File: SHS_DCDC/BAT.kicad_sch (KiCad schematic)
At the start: 11 parts, among them Q10 PMV100XPEAR, Q11 PMV100XPEAR, Q12 PMV100XPEAR, Q17 MOSP_GENERIC, Q9 PMV100XPEAR, U2 INA181, U7 MCP101

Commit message: Ubuntu transfer
Commit before transfer onto Ubuntu
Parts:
- removed Q17: MOSP_GENERIC, Package_TO_SOT_SMD:SOT-23, symbol SHS_DCDC:MOSP_GENERIC
- added Q17: PMV100XPEAR, digikey-kicad-library-master:SOT-23-3, symbol SHS_DCDC:PMV100XPEAR
- Q12: footprint digikey-footprints:SOT-23-3 -> digikey-kicad-library-master:SOT-23-3
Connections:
- net ODP_RESET: now also Q17.1 (G)
- net VBAT: now also Q17.2 (S)
- net at R8.1, U2.3 (+): now also Q17.3 (D)
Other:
- note added: "THAT VOLTAGE DETECTOR SENSE THE BATTERY'S VOLTAGE. IF VBAT GOES BELOW A CERTAIN VOLTAGE, IT TRIGGERS A POSITIVE VALUE. THAT POSITIVE VALUE BLOCKS THE DRAIN OF THE BATTERY."
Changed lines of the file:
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@@
     (stroke (width 0) (type default) (color 0 0 0 0))
   )
-  (wire (pts (xy 198.12 118.11) (xy 209.55 118.11))
+  (wire (pts (xy 198.12 120.65) (xy 208.28 120.65))
     (stroke (width 0) (type default) (color 0 0 0 0))
   )
@@
     (stroke (width 0) (type default) (color 0 0 0 0))
   )
-  (wire (pts (xy 217.17 97.79) (xy 217.17 115.57))
+  (wire (pts (xy 217.17 97.79) (xy 217.17 113.03))
     (stroke (width 0) (type default) (color 0 0 0 0))
   )
@@
     (stroke (width 0) (type default) (color 0 0 0 0))
   )
-  (wire (pts (xy 217.17 125.73) (xy 217.17 137.16))
+  (wire (pts (xy 217.17 123.19) (xy 217.17 137.16))
     (stroke (width 0) (type default) (color 0 0 0 0))
   )
@@
     (effects (font (size 1.27 1.27)) (justify left bottom))
   )
+  (text "THAT VOLTAGE DETECTOR SENSE THE BATTERY'S VOLTAGE.\nIF VBAT GOES BELOW A CERTAIN VOLTAGE, IT TRIGGERS A POSITIVE VALUE.\nTHAT POSITIVE VALUE BLOCKS THE DRAIN OF THE BATTERY."
+    (at 80.01 43.18 0)
+    (effects (font (size 1.27 1.27)) (justify left bottom))
+  )
   (text "INSTRUM AMPLIFIER BLOCK\nVREF_BIDIRECTIONAL IS HALF THE VDD OF THE MCU\nTHAT MEANS THE OUTPUT VALUE WILL VARY AROUND THAT EQUILIBRIUM POINT\nBELOW OR HIGHER THAN VDD/2 WILL DEFINE BIDIRECTIONALITY OF THE BATTERY CURRENT\nEG, IF THE BATTERY IS DISCHARGING OR CHARGING\nSEE INA181 DATASHEET FOR MORE INFO"
     (at 146.05 58.42 0)
     (effects (font (size 1.27 1.27)) (justify left bottom))
   )
-  (global_label "USB_IN" (shape input) (at 262.89 46.99 0) (fields_autoplaced)
+  (global_label "USB_IN" (shape input) (at 261.62 46.99 0) (fields_autoplaced)
     (effects (font (size 1.27 1.27)) (justify left))
-    (property "Intersheet References" "${INTERSHEET_REFS}" (id 0) (at 288.29 -176.53 0)
+    (property "Intersheet References" "${INTERSHEET_REFS}" (id 0) (at 287.02 -176.53 0)
       (effects (font (size 1.27 1.27)) hide)
     )
@@
     )
   )
-  (global_label "ODP_RESET" (shape input) (at 198.12 118.11 180) (fields_autoplaced)
+  (global_label "ODP_RESET" (shape input) (at 198.12 120.65 180) (fields_autoplaced)
     (effects (font (size 1.27 1.27)) (justify right))
-    (property "Intersheet References" "${INTERSHEET_REFS}" (id 0) (at 185.2125 118.0306 0)
+    (property "Intersheet References" "${INTERSHEET_REFS}" (id 0) (at 185.2125 120.5706 0)
       (effects (font (size 1.27 1.27)) (justify right) hide)
     )
@@
       (effects (font (size 1.524 1.524)) (justify left))
     )
-    (property "Footprint" "digikey-footprints:SOT-23-3" (id 2) (at 110.49 129.54 0)
+    (property "Footprint" "digikey-kicad-library-master:SOT-23-3" (id 2) (at 110.49 129.54 0)
       (effects (font (size 1.524 1.524)) (justify left) hide)
     )
@@
     )
     (pin "1")
+  )
+  (symbol (lib_id "SHS_DCDC:PMV100XPEAR") (at 217.17 118.11 0) (unit 1)
+    (in_bom yes) (on_board yes) (fields_autoplaced)
+    (property "Reference" "Q17" (id 0) (at 220.98 118.2997 0)
+      (effects (font (size 1.524 1.524)) (justify left))
+    )
+    (property "Value" "PMV100XPEAR" (id 1) (at 220.98 122.1097 0)
+      (effects (font (size 1.524 1.524)) (justify left))
+    )
+    (property "Footprint" "digikey-kicad-library-master:SOT-23-3" (id 2) (at 222.25 113.03 0)
+      (effects (font (size 1.524 1.524)) (justify left) hide)
+    )
+    (property "Datasheet" "" (id 3) (at 222.25 110.49 0)
+      (effects (font (size 1.524 1.524)) (justify left) hide)
+    )
+    (property "MPN" "PMV100XPEAR" (id 4) (at 222.25 105.41 0)
+      (effects (font (size 1.524 1.524)) (justify left) hide)
+    )
+    (property "Category" "Discrete Semiconductor Products" (id 5) (at 222.25 102.87 0)
+      (effects (font (size 1.524 1.524)) (justify left) hide)
+    )
+    (property "Family" "Transistors - FETs, MOSFETs - Single" (id 6) (at 222.25 100.33 0)
+      (effects (font (size 1.524 1.524)) (justify left) hide)
+    )
+    (property "Description" "MOSFET P-CH 20V 2.4A SOT23" (id 7) (at 222.25 97.79 0)
+      (effects (font (size 1.524 1.524)) (justify left) hide)
+    )
+    (property "Manufacturer" "Nexperia USA" (id 8) (at 222.25 95.25 0)
+      (effects (font (size 1.524 1.524)) (justify left) hide)
+    )
+    (property "Status" "Active" (id 9) (at 222.25 92.71 0)
+      (effects (font (size 1.524 1.524)) (justify left) hide)
+    )
+    (pin "1")
+    (pin "2")
+    (pin "3")
   )
   (symbol (lib_id "SHS_DCDC:C-Device") (at 55.88 44.45 0) (unit 1)
@@
     (pin "1")
   )
-  (symbol (lib_id "SHS_DCDC:MOSP_GENERIC") (at 217.17 120.65 0) (mirror x) (unit 1)
-    (in_bom yes) (on_board yes) (fields_autoplaced)
-    (property "Reference" "Q17" (id 0) (at 220.98 119.38 0)
-      (effects (font (size 1.524 1.524)) (justify left))
-    )
-    (property "Value" "MOSP_GENERIC" (id 1) (at 220.98 123.19 0)
-      (effects (font (size 1.524 1.524)) (justify left))
-    )
-    (property "Footprint" "Package_TO_SOT_SMD:SOT-23" (id 2) (at 222.25 125.73 0)
-      (effects (font (size 1.524 1.524)) (justify left) hide)
-    )
-    (property "Datasheet" "https://www.onsemi.com/pub/Collateral/NDS7002A-D.PDF" (id 3) (at 222.25 128.27 0)
-      (effects (font (size 1.524 1.524)) (justify left) hide)
-    )
-    (property "Digi-Key_PN" "2N7002NCT-ND" (id 4) (at 222.25 130.81 0)
-      (effects (font (size 1.524 1.524)) (justify left) hide)
-    )
-    (property "MPN" "2N7002" (id 5) (at 222.25 133.35 0)
-      (effects (font (size 1.524 1.524)) (justify left) hide)
-    )
-    (property "Category" "Discrete Semiconductor Products" (id 6) (at 222.25 135.89 0)
-      (effects (font (size 1.524 1.524)) (justify left) hide)
-    )
-    (property "Family" "Transistors - FETs, MOSFETs - Single" (id 7) (at 222.25 138.43 0)
-      (effects (font (size 1.524 1.524)) (justify left) hide)
-    )
-    (property "DK_Datasheet_Link" "https://www.onsemi.com/pub/Collateral/NDS7002A-D.PDF" (id 8) (at 222.25 140.97 0)
-      (effects (font (size 1.524 1.524)) (justify left) hide)
-    )
-    (property "DK_Detail_Page" "/product-detail/en/on-semiconductor/2N7002/2N7002NCT-ND/244664" (id 9) (at 222.25 143.51 0)
-      (effects (font (size 1.524 1.524)) (justify left) hide)
-    )
-    (property "Description" "MOSFET N-CH 60V 115MA SOT-23" (id 10) (at 222.25 146.05 0)
-      (effects (font (size 1.524 1.524)) (justify left) hide)
-    )
-    (property "Manufacturer" "ON Semiconductor" (id 11) (at 222.25 148.59 0)
-      (effects (font (size 1.524 1.524)) (justify left) hide)
-    )
-    (property "Status" "Active" (id 12) (at 222.25 151.13 0)
-      (effects (font (size 1.524 1.524)) (justify left) hide)
-    )
-    (pin "1")
-    (pin "2")
-    (pin "3")
-  )
   (symbol (lib_id "SHS_DCDC:GND-power") (at 55.88 54.61 0) (unit 1)

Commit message: Commit_190223
Normal commit
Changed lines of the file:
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@@
   (junction (at 217.17 76.2) (diameter 0) (color 0 0 0 0)
   )
-  (junction (at 233.68 30.48) (diameter 0) (color 0 0 0 0)
-  )
-  (junction (at 217.17 30.48) (diameter 0) (color 0 0 0 0)
-  )
   (junction (at 55.88 36.83) (diameter 0) (color 0 0 0 0)
   )
@@
     (stroke (width 0) (type default) (color 0 0 0 0))
   )
-  (wire (pts (xy 261.62 46.99) (xy 233.68 46.99))
-    (stroke (width 0) (type default) (color 0 0 0 0))
-  )
   (wire (pts (xy 217.17 76.2) (xy 217.17 83.82))
     (stroke (width 0) (type default) (color 0 0 0 0))
@@
     (stroke (width 0) (type default) (color 0 0 0 0))
   )
-  (wire (pts (xy 35.56 30.48) (xy 217.17 30.48))
-    (stroke (width 0) (type default) (color 0 0 0 0))
-  )
   (wire (pts (xy 55.88 48.26) (xy 55.88 54.61))
     (stroke (width 0) (type default) (color 0 0 0 0))
@@
     (stroke (width 0) (type default) (color 0 0 0 0))
   )
-  (wire (pts (xy 217.17 30.48) (xy 233.68 30.48))
-    (stroke (width 0) (type default) (color 0 0 0 0))
-  )
   (wire (pts (xy 95.25 171.45) (xy 95.25 181.61))
     (stroke (width 0) (type default) (color 0 0 0 0))
@@
     (stroke (width 0) (type default) (color 0 0 0 0))
   )
-  (wire (pts (xy 233.68 30.48) (xy 262.89 30.48))
-    (stroke (width 0) (type default) (color 0 0 0 0))
-  )
   (wire (pts (xy 115.57 151.13) (xy 95.25 151.13))
     (stroke (width 0) (type default) (color 0 0 0 0))
@@
   )
   (wire (pts (xy 46.99 151.13) (xy 64.77 151.13))
-    (stroke (width 0) (type default) (color 0 0 0 0))
-  )
-  (wire (pts (xy 233.68 46.99) (xy 233.68 30.48))
     (stroke (width 0) (type default) (color 0 0 0 0))
   )
@@
     (at 146.05 58.42 0)
     (effects (font (size 1.27 1.27)) (justify left bottom))
-  )
-  (global_label "USB_IN" (shape input) (at 261.62 46.99 0) (fields_autoplaced)
-    (effects (font (size 1.27 1.27)) (justify left))
-    (property "Intersheet References" "${INTERSHEET_REFS}" (id 0) (at 287.02 -176.53 0)
-      (effects (font (size 1.27 1.27)) hide)
-    )
   )
   (global_label "VREF_BIDIRECTIONAL" (shape input) (at 133.35 72.39 180) (fields_autoplaced)
@@
     )
   )
-  (global_label "LOAD" (shape output) (at 262.89 30.48 0) (fields_autoplaced)
-    (effects (font (size 1.27 1.27)) (justify left))
-    (property "Intersheet References" "${INTERSHEET_REFS}" (id 0) (at 0 -7.62 0)
-      (effects (font (size 1.27 1.27)) hide)
-    )
-  )
   (global_label "V_MCU" (shape input) (at 152.4 104.14 270) (fields_autoplaced)
     (effects (font (size 1.27 1.27)) (justify right))
@@
     )
   )
-  (global_label "V1" (shape input) (at 35.56 30.48 180) (fields_autoplaced)
-    (effects (font (size 1.27 1.27)) (justify right))
-    (property "Intersheet References" "${INTERSHEET_REFS}" (id 0) (at 30.9377 30.4006 0)
-      (effects (font (size 1.27 1.27)) (justify right) hide)
-    )
-  )
+  (global_label "LOAD" (shape input) (at 217.17 30.48 90) (fields_autoplaced)
+    (effects (font (size 1.27 1.27)) (justify left))
+    (property "Intersheet References" "${INTERSHEET_REFS}" (id 0) (at 217.2494 23.4387 90)
+      (effects (font (size 1.27 1.27)) (justify left) hide)
+    )
+  )

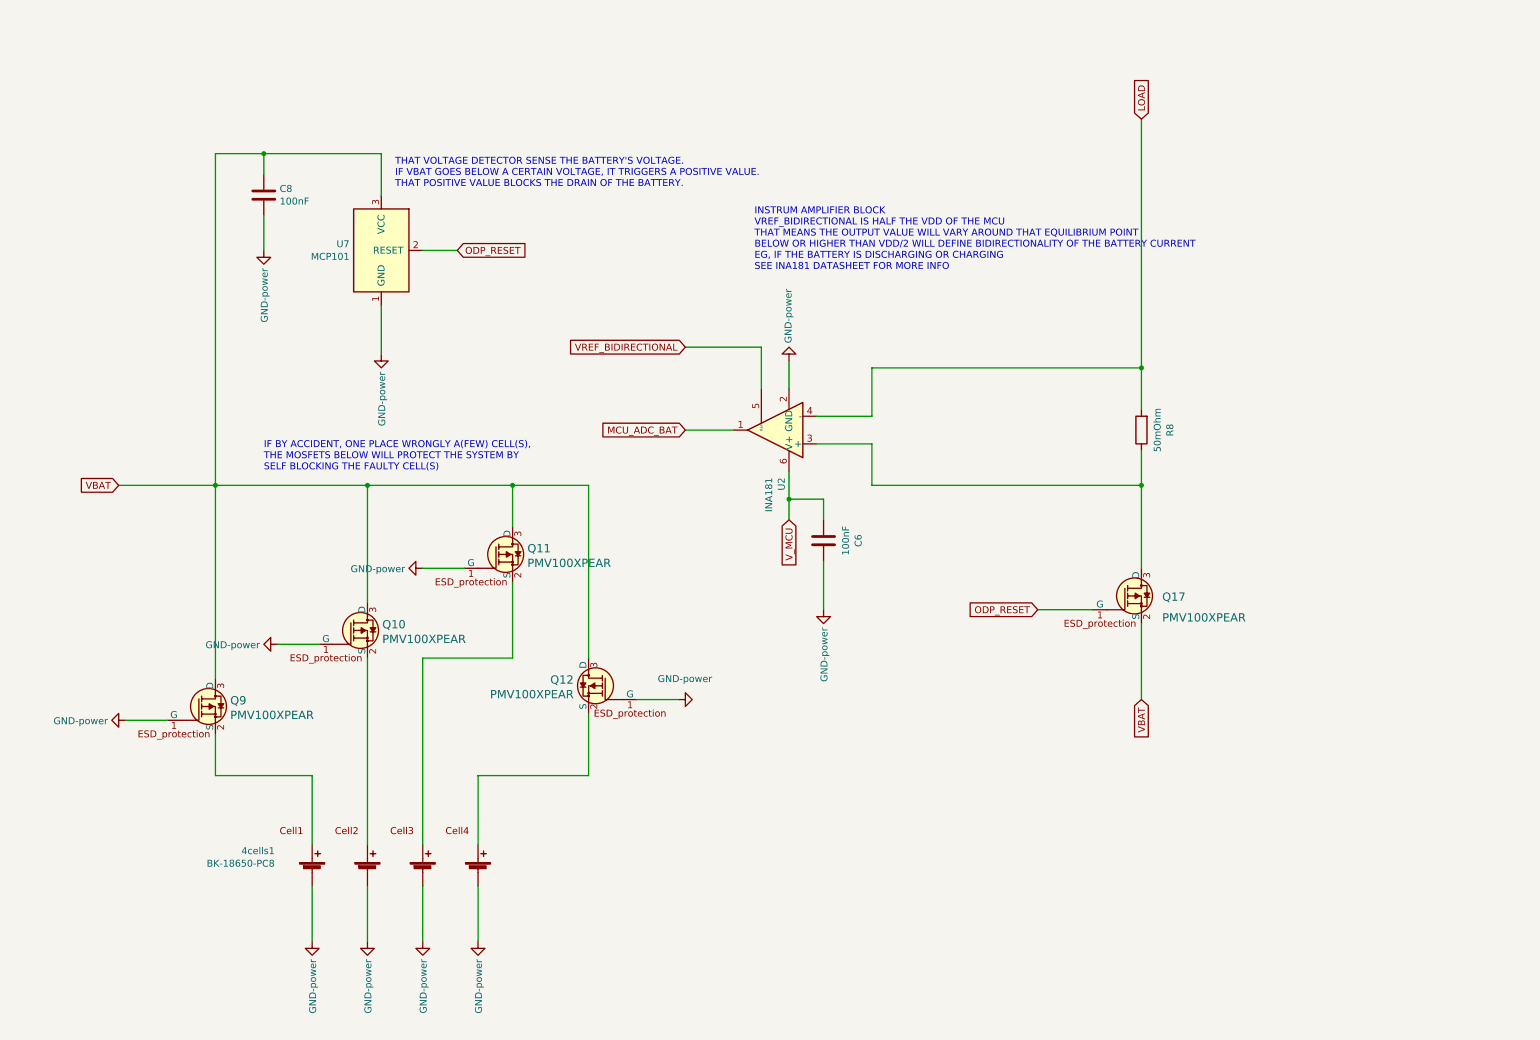
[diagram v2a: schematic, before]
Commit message: Commit_Fix
Fix to move back to ESP32
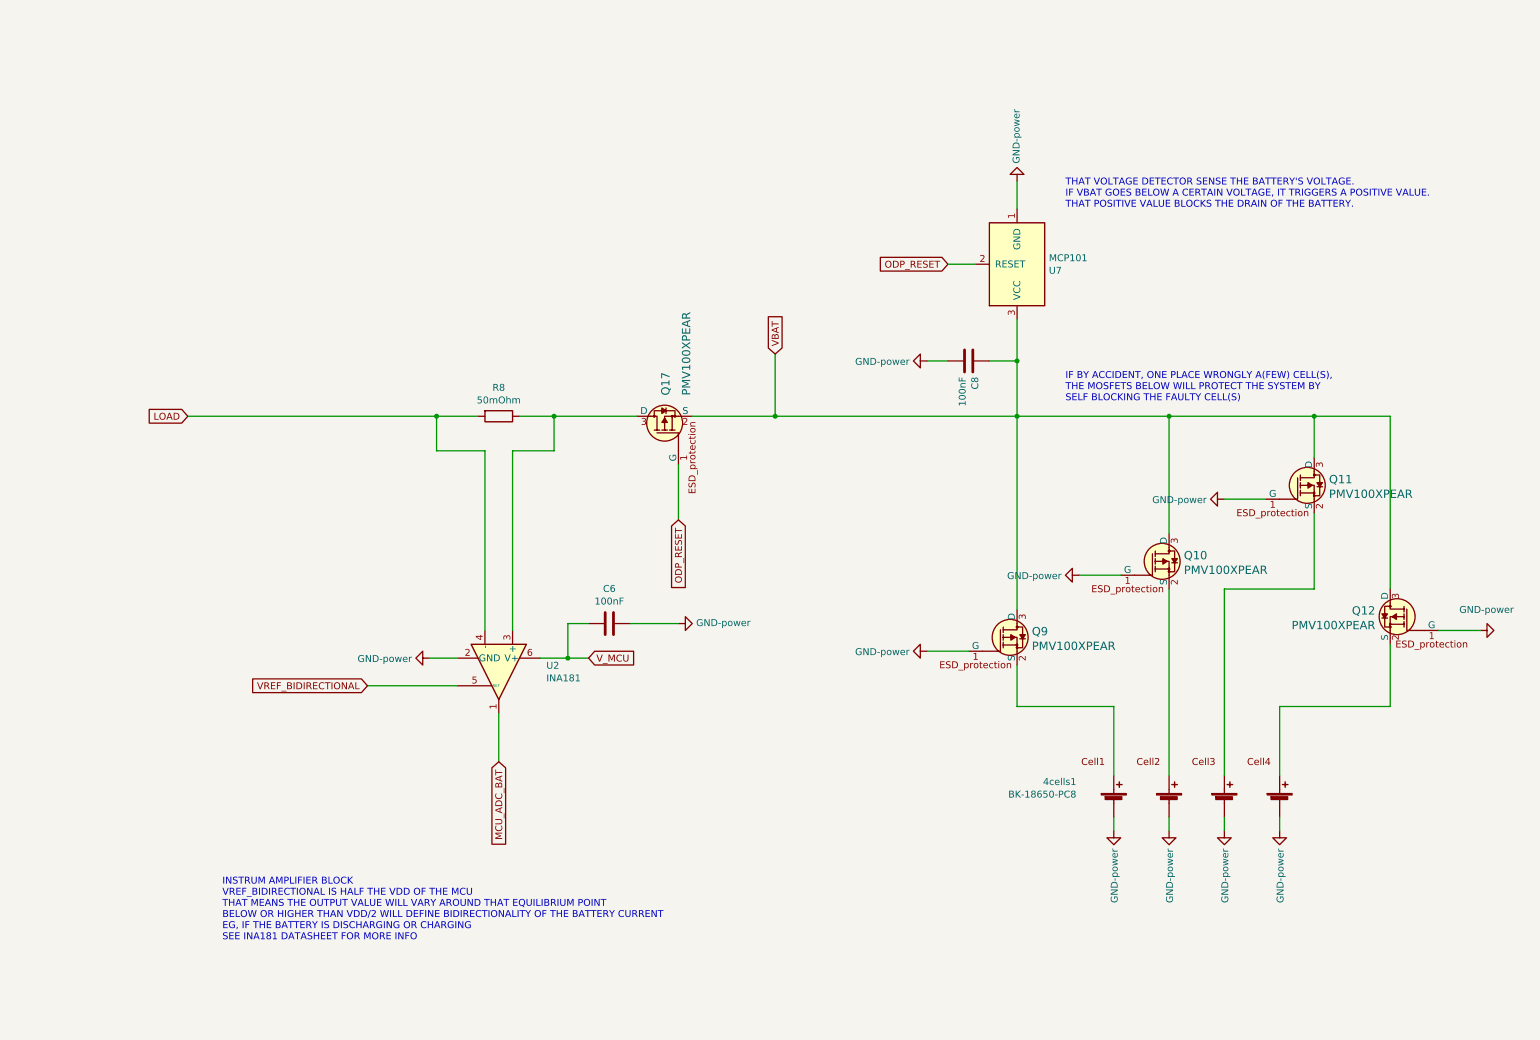
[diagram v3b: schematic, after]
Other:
- moved on the sheet: 4cells1, C6, C8, Q10, Q11, Q12, Q17, Q9, R8, U2, U7

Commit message: ProgressMisc
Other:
- moved on the sheet: 4cells1, C6, C8, Q10, Q11, Q12, Q17, Q9, R8, U2, U7

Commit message: OCP
Adding overcharge protection
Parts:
- added C38: 100nF, Capacitor_SMD:C_0402_1005Metric, symbol SHS_DCDC:C-Device
- added Q13: PMV100XPEAR, digikey-kicad-library-master:SOT-23-3, symbol SHS_DCDC:PMV100XPEAR
- added R25: 100k, Resistor_SMD:R_0402_1005Metric, symbol Device:R
- added U9: BD49LxxG, Package_TO_SOT_SMD:SOT-23, symbol Power_Management:BD49LxxG
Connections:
- net GND: now also C38.2, U9.3 (GND)
- net VBAT_SW: now reaches R8.1, U2.3 (+)
- net VBAT_SW: now also C38.1, Q13.2 (S), U9.2 (VDD); no longer Q17.3 (D)
- new net: Q13.3 (D), Q17.3 (D)
- new net MCU_OCP_BAT: R25.1
- new net OCP_BAT: Q13.1 (G), R25.2, U9.1 (VOUT)
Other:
- moved on the sheet: C6, Q17, R8, U2
